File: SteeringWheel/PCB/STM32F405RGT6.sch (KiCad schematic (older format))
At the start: 21 parts, among them J14 SWD, SW1 SW_SPDT, U6 STM32F405RGT6, Y1 16MHz

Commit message: Steering Wheel Update
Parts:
- Y1: footprint Crystal:Crystal_SMD_3225-4Pin_3.2x2.5mm -> PGR-06_Additional:SODFL5326X110N
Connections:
- net BTN_CLCH: now also U6.26 (PB0); no longer U6.59 (PB7)
- net BTN_DRS: now also U6.28 (PB2); no longer U6.58 (PB6)
- net BTN_PTT: now also U6.25 (PC5); no longer U6.61 (PB8)
- net BTN_SCR: now also U6.24 (PC4); no longer U6.62 (PB9)
- net BTN_UNI1: now also U6.27 (PB1); no longer U6.57 (PB5)
- net BTN_UNI2: now also U6.37 (PC6); no longer U6.29 (PB10)
- net ROT_SCR: now also U6.15 (PA1); no longer U6.3 (PC14)
- net ROT_UNI: now also U6.14 (PA0); no longer U6.4 (PC15)
- new net I2C_RESET: U6.57 (PB5)
- new net I2C_SCL: U6.58 (PB6)
- new net I2C_SDA: U6.59 (PB7)
- no-connect marks 32 -> 31
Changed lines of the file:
@@
 $Descr A4 11693 8268
 encoding utf-8
-Sheet 2 4
+Sheet 2 3
 Title ""
 Date ""
@@
 F 0 "Y1" H 6525 4250 50  0000 L CNN
 F 1 "16MHz" H 6450 4150 50  0000 L CNN
-F 2 "Crystal:Crystal_SMD_3225-4Pin_3.2x2.5mm" H 6575 3925 50  0001 C CNN
+F 2 "PGR-06_Additional:SODFL5326X110N" H 6575 3925 50  0001 C CNN
 F 3 "~" H 6575 3925 50  0001 C CNN
 F 4 "C13738" H 6575 3925 50  0001 C CNN "LCSC Part #"
@@
 	0    -1   -1   0
 $EndComp
-NoConn ~ 3500 5475
 NoConn ~ 3500 5375
 NoConn ~ 3500 5275
 NoConn ~ 3500 5175
 NoConn ~ 3500 4875
-NoConn ~ 3500 4775
-NoConn ~ 3500 4675
-NoConn ~ 3500 4575
-NoConn ~ 3500 4475
-NoConn ~ 3500 4375
-NoConn ~ 3500 4275
 NoConn ~ 3500 4175
 NoConn ~ 3500 3975
 NoConn ~ 4900 4575
-NoConn ~ 4900 4375
-NoConn ~ 4900 3975
 NoConn ~ 4900 3475
 NoConn ~ 4900 3375
@@
 NoConn ~ 4900 2875
 NoConn ~ 4900 2775
-NoConn ~ 4900 2575
 Text GLabel 3500 3775 0    50   Input ~ 0
 HSE_OUT
@@
 Text GLabel 4900 2675 2    50   Input ~ 0
 LED_STATUS
-Text GLabel 4900 3775 2    50   Input ~ 0
-SWDIO
-Text GLabel 4900 3875 2    50   Input ~ 0
-SWCLK
 Text GLabel 4900 4475 2    50   Input ~ 0
 SWO
 Text HLabel 4900 3575 2    50   Input ~ 0
 CAN1_RX
-Text HLabel 4900 3675 2    50   Input ~ 0
-CAN1_TX
 Text HLabel 4900 5375 2    50   Input ~ 0
 CAN2_RX
 Text HLabel 4900 5475 2    50   Input ~ 0
 CAN2_TX
+Text HLabel 3500 4675 0    50   Input ~ 0
+BTN_PTT
+Text HLabel 3500 4575 0    50   Input ~ 0
+BTN_SCR
+Text HLabel 3500 4775 0    50   Input ~ 0
+BTN_UNI2
+Text HLabel 3500 4975 0    50   Input ~ 0
+LED_DATA
+NoConn ~ 3500 5075
+NoConn ~ 4900 5275
+Text HLabel 4900 4175 2    50   Input ~ 0
+BTN_CLCH
+Text HLabel 4900 4275 2    50   Input ~ 0
+BTN_UNI1
+Text HLabel 4900 4375 2    50   Input ~ 0
+BTN_DRS
 Text HLabel 4900 4775 2    50   Input ~ 0
-BTN_DRS
+I2C_SCL
 Text HLabel 4900 4875 2    50   Input ~ 0
-BTN_CLCH
-Text HLabel 4900 4975 2    50   Input ~ 0
-BTN_PTT
-Text HLabel 4900 5075 2    50   Input ~ 0
-BTN_SCR
+I2C_SDA
+Text HLabel 4900 4675 2    50   Input ~ 0
+I2C_RESET
+Text HLabel 4900 3675 2    50   Input ~ 0
+CAN1_TX
+Text GLabel 4900 3875 2    50   Input ~ 0
+SWCLK
+Text GLabel 4900 3775 2    50   Input ~ 0
+SWDIO
+NoConn ~ 4900 3975
 $Comp
 L MCU_ST_STM32F4:STM32F405RGTx U6
@@
 	1    0    0    -1
 $EndComp
-Text HLabel 4900 4675 2    50   Input ~ 0
-BTN_UNI1
-Text HLabel 4900 5175 2    50   Input ~ 0
-BTN_UNI2
-Text HLabel 3500 5575 0    50   Input ~ 0
+Text HLabel 4900 2475 2    50   Input ~ 0
+ROT_UNI
+Text HLabel 4900 2575 2    50   Input ~ 0
 ROT_SCR
-Text HLabel 3500 5675 0    50   Input ~ 0
-ROT_UNI
-Text HLabel 3500 4975 0    50   Input ~ 0
-LED_DATA
-NoConn ~ 3500 5075
-NoConn ~ 4900 5275
-NoConn ~ 4900 4175
-NoConn ~ 4900 4275
+NoConn ~ 3500 5475
+NoConn ~ 4900 4975
+NoConn ~ 4900 5075
+NoConn ~ 4900 5175
+NoConn ~ 3500 5575
+NoConn ~ 3500 5675
+NoConn ~ 3500 4275
+NoConn ~ 3500 4375
+NoConn ~ 3500 4475
+NoConn ~ 4900 3075
+Text HLabel 4200 2250 1    50   Input ~ 0
+VDD
+Text HLabel 4200 5900 3    50   Input ~ 0
+VSS
 $EndSCHEMATC

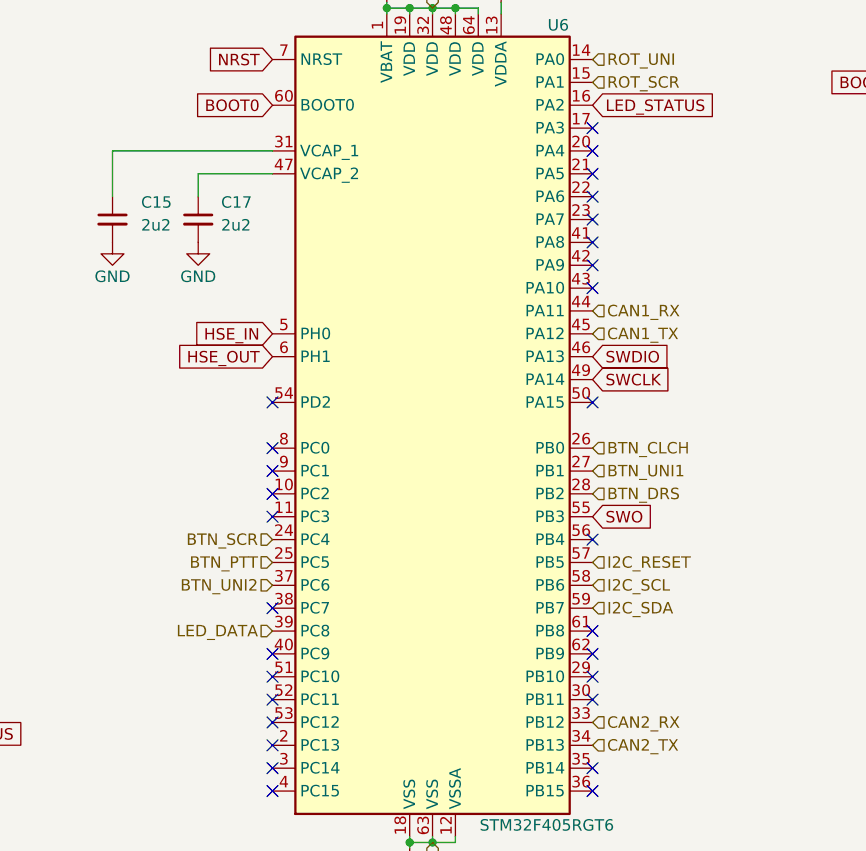
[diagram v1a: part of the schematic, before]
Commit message: New brd for steering wheel
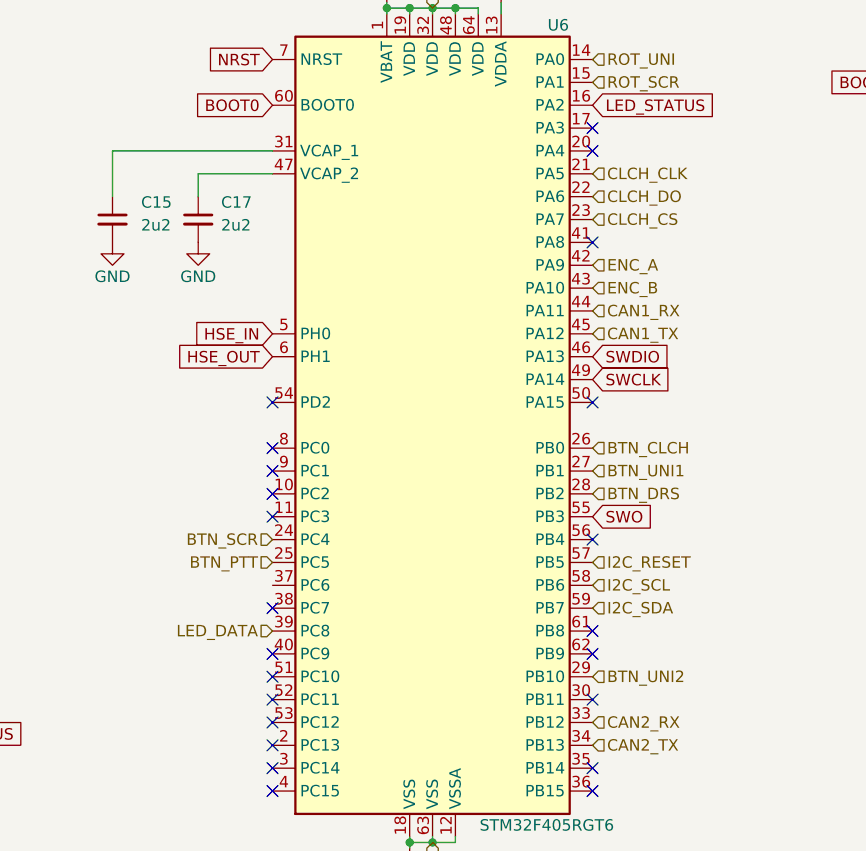
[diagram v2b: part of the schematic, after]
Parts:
- C15, C16, C17: footprint Capacitor_SMD:C_0603_1608Metric -> Capacitor_SMD:C_0805_2012Metric
- C18, C19, C20, C21, C22, C23, C24, C25, C26: footprint Capacitor_SMD:C_0402_1005Metric -> Capacitor_SMD:C_0805_2012Metric
- R15: footprint Resistor_SMD:R_0603_1608Metric -> Resistor_SMD:R_0805_2012Metric
- R16, R17: footprint Resistor_SMD:R_0402_1005Metric -> Resistor_SMD:R_0805_2012Metric
- Y1: footprint PGR-06_Additional:SODFL5326X110N -> PGR-06_Additional:OSCCC500X320X110-4N
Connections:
- net BTN_UNI2: now also U6.29 (PB10); no longer U6.37 (PC6)
- net CLCH_CLK: now reaches U6.21 (PA5)
- net CLCH_DO: now reaches U6.22 (PA6)
- net CLCH_CS: now reaches U6.23 (PA7)
- net ENC_A: now reaches U6.42 (PA9)
- net ENC_B: now reaches U6.43 (PA10)
- no-connect marks 31 -> 25
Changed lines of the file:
@@
 $Descr A4 11693 8268
 encoding utf-8
-Sheet 2 3
+Sheet 3 3
 Title ""
 Date ""
@@
 F 0 "R16" V 6300 2575 50  0000 C CNN
 F 1 "10k" V 6450 2575 50  0000 C CNN
-F 2 "Resistor_SMD:R_0402_1005Metric" H 6375 2575 50  0001 C CNN
+F 2 "Resistor_SMD:R_0805_2012Metric" H 6375 2575 50  0001 C CNN
 F 3 "~" H 6375 2575 50  0001 C CNN
 F 4 "C25744" H 6375 2575 50  0001 C CNN "LCSC Part #"
@@
 F 0 "C16" H 3175 1525 50  0000 L CNN
 F 1 "4u7" H 3175 1425 50  0000 L CNN
-F 2 "Capacitor_SMD:C_0603_1608Metric" H 3075 1475 50  0001 C CNN
+F 2 "Capacitor_SMD:C_0805_2012Metric" H 3075 1475 50  0001 C CNN
 F 3 "~" H 3075 1475 50  0001 C CNN
 F 4 "C19666" H 3075 1475 50  0001 C CNN "LCSC Part #"
@@
 F 0 "C18" H 3525 1525 50  0000 L CNN
 F 1 "100n" H 3525 1425 50  0000 L CNN
-F 2 "Capacitor_SMD:C_0402_1005Metric" H 3425 1475 50  0001 C CNN
+F 2 "Capacitor_SMD:C_0805_2012Metric" H 3425 1475 50  0001 C CNN
 F 3 "~" H 3425 1475 50  0001 C CNN
 F 4 "C1525" H 3425 1475 50  0001 C CNN "LCSC Part #"
@@
 F 0 "C19" H 3900 1525 50  0000 L CNN
 F 1 "100n" H 3900 1425 50  0000 L CNN
-F 2 "Capacitor_SMD:C_0402_1005Metric" H 3800 1475 50  0001 C CNN
+F 2 "Capacitor_SMD:C_0805_2012Metric" H 3800 1475 50  0001 C CNN
 F 3 "~" H 3800 1475 50  0001 C CNN
 F 4 "C1525" H 3800 1475 50  0001 C CNN "LCSC Part #"
@@
 F 0 "C20" H 4275 1525 50  0000 L CNN
 F 1 "100n" H 4275 1425 50  0000 L CNN
-F 2 "Capacitor_SMD:C_0402_1005Metric" H 4175 1475 50  0001 C CNN
+F 2 "Capacitor_SMD:C_0805_2012Metric" H 4175 1475 50  0001 C CNN
 F 3 "~" H 4175 1475 50  0001 C CNN
 F 4 "C1525" H 4175 1475 50  0001 C CNN "LCSC Part #"
@@
 F 0 "C21" H 4650 1525 50  0000 L CNN
 F 1 "100n" H 4650 1425 50  0000 L CNN
-F 2 "Capacitor_SMD:C_0402_1005Metric" H 4550 1475 50  0001 C CNN
+F 2 "Capacitor_SMD:C_0805_2012Metric" H 4550 1475 50  0001 C CNN
 F 3 "~" H 4550 1475 50  0001 C CNN
 F 4 "C1525" H 4550 1475 50  0001 C CNN "LCSC Part #"
@@
 F 0 "C22" H 5025 1525 50  0000 L CNN
 F 1 "100n" H 5025 1425 50  0000 L CNN
-F 2 "Capacitor_SMD:C_0402_1005Metric" H 4925 1475 50  0001 C CNN
+F 2 "Capacitor_SMD:C_0805_2012Metric" H 4925 1475 50  0001 C CNN
 F 3 "~" H 4925 1475 50  0001 C CNN
 F 4 "C1525" H 4925 1475 50  0001 C CNN "LCSC Part #"
@@
 F 0 "C23" H 6175 1525 50  0000 L CNN
 F 1 "1u" H 6175 1425 50  0000 L CNN
-F 2 "Capacitor_SMD:C_0402_1005Metric" H 6075 1475 50  0001 C CNN
+F 2 "Capacitor_SMD:C_0805_2012Metric" H 6075 1475 50  0001 C CNN
 F 3 "~" H 6075 1475 50  0001 C CNN
 F 4 "C52923" H 6075 1475 50  0001 C CNN "LCSC Part #"
@@
 F 0 "C25" H 6500 1525 50  0000 L CNN
 F 1 "10n" H 6500 1425 50  0000 L CNN
-F 2 "Capacitor_SMD:C_0402_1005Metric" H 6400 1475 50  0001 C CNN
+F 2 "Capacitor_SMD:C_0805_2012Metric" H 6400 1475 50  0001 C CNN
 F 3 "~" H 6400 1475 50  0001 C CNN
 F 4 "C15195" H 6400 1475 50  0001 C CNN "LCSC Part #"
@@
 F 0 "Y1" H 6525 4250 50  0000 L CNN
 F 1 "16MHz" H 6450 4150 50  0000 L CNN
-F 2 "PGR-06_Additional:SODFL5326X110N" H 6575 3925 50  0001 C CNN
+F 2 "PGR-06_Additional:OSCCC500X320X110-4N" H 6575 3925 50  0001 C CNN
 F 3 "~" H 6575 3925 50  0001 C CNN
 F 4 "C13738" H 6575 3925 50  0001 C CNN "LCSC Part #"
@@
 F 0 "C26" H 6925 4250 50  0000 L CNN
 F 1 "12p" H 6925 4150 50  0000 L CNN
-F 2 "Capacitor_SMD:C_0402_1005Metric" H 6825 4175 50  0001 C CNN
+F 2 "Capacitor_SMD:C_0805_2012Metric" H 6825 4175 50  0001 C CNN
 F 3 "~" H 6825 4175 50  0001 C CNN
 F 4 "C1547" H 6825 4175 50  0001 C CNN "LCSC Part #"
@@
 F 0 "C24" H 6425 4250 50  0000 L CNN
 F 1 "12p" H 6425 4150 50  0000 L CNN
-F 2 "Capacitor_SMD:C_0402_1005Metric" H 6325 4175 50  0001 C CNN
+F 2 "Capacitor_SMD:C_0805_2012Metric" H 6325 4175 50  0001 C CNN
 F 3 "~" H 6325 4175 50  0001 C CNN
 F 4 "C1547" H 6325 4175 50  0001 C CNN "LCSC Part #"
@@
 F 0 "R17" H 6900 3700 50  0000 L CNN
 F 1 "47" H 6900 3600 50  0000 L CNN
-F 2 "Resistor_SMD:R_0402_1005Metric" H 6825 3650 50  0001 C CNN
+F 2 "Resistor_SMD:R_0805_2012Metric" H 6825 3650 50  0001 C CNN
 F 3 "~" H 6825 3650 50  0001 C CNN
 F 4 "C25118" H 6825 3650 50  0001 C CNN "LCSC Part #"
@@
 F 0 "R15" H 1675 5875 50  0000 C CNN
 F 1 "1k5" H 1650 5975 50  0000 C CNN
-F 2 "Resistor_SMD:R_0603_1608Metric" H 1775 5925 50  0001 C CNN
+F 2 "Resistor_SMD:R_0805_2012Metric" H 1775 5925 50  0001 C CNN
 F 3 "~" H 1775 5925 50  0001 C CNN
 F 4 "C22843" H 1775 5925 50  0001 C CNN "LCSC Part #"
@@
 NoConn ~ 3500 3975
 NoConn ~ 4900 4575
-NoConn ~ 4900 3475
-NoConn ~ 4900 3375
 NoConn ~ 4900 3275
-NoConn ~ 4900 3175
-NoConn ~ 4900 2975
-NoConn ~ 4900 2875
 NoConn ~ 4900 2775
 Text GLabel 3500 3775 0    50   Input ~ 0
@@
 F 0 "C15" H 2925 3250 50  0000 L CNN
 F 1 "2u2" H 2925 3150 50  0000 L CNN
-F 2 "Capacitor_SMD:C_0603_1608Metric" H 2800 3175 50  0001 C CNN
+F 2 "Capacitor_SMD:C_0805_2012Metric" H 2800 3175 50  0001 C CNN
 F 3 "~" H 2800 3175 50  0001 C CNN
 F 4 "C23630" H 2800 3175 50  0001 C CNN "LCSC Part #"
@@
 F 0 "C17" H 3275 3250 50  0000 L CNN
 F 1 "2u2" H 3275 3150 50  0000 L CNN
-F 2 "Capacitor_SMD:C_0603_1608Metric" H 3175 3175 50  0001 C CNN
+F 2 "Capacitor_SMD:C_0805_2012Metric" H 3175 3175 50  0001 C CNN
 F 3 "~" H 3175 3175 50  0001 C CNN
 F 4 "C23630" H 3175 3175 50  0001 C CNN "LCSC Part #"
@@
 Text HLabel 3500 4575 0    50   Input ~ 0
 BTN_SCR
-Text HLabel 3500 4775 0    50   Input ~ 0
+Text HLabel 4900 5175 2    50   Input ~ 0
 BTN_UNI2
 Text HLabel 3500 4975 0    50   Input ~ 0
@@
 NoConn ~ 4900 4975
 NoConn ~ 4900 5075
-NoConn ~ 4900 5175
 NoConn ~ 3500 5575
 NoConn ~ 3500 5675
@@
 NoConn ~ 3500 4375
 NoConn ~ 3500 4475
-NoConn ~ 4900 3075
 Text HLabel 4200 2250 1    50   Input ~ 0
 VDD
 Text HLabel 4200 5900 3    50   Input ~ 0
 VSS
+Text HLabel 4900 3375 2    50   Input ~ 0
+ENC_A
+Text HLabel 4900 3475 2    50   Input ~ 0
+ENC_B
+NoConn ~ 4900 2875
+Text HLabel 4900 3075 2    50   Input ~ 0
+CLCH_DO
+Text HLabel 4900 2975 2    50   Input ~ 0
+CLCH_CLK
+Text HLabel 4900 3175 2    50   Input ~ 0
+CLCH_CS
 $EndSCHEMATC

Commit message: Steering Wheel Update
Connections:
- net ROT_SCR: now also U6.41 (PA8); no longer U6.15 (PA1)
- net ROT_UNI: now also U6.40 (PC9); no longer U6.14 (PA0)
- net LED_B: now reaches U6.35 (PB14)
- net LED_G: now reaches U6.36 (PB15)
- net LED_R: now reaches U6.37 (PC6)
- net LED_DATA: no longer names the net of U6.39 (PC8)
- no-connect marks 25 -> 24
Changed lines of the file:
@@
 NoConn ~ 3500 5175
 NoConn ~ 3500 4875
-NoConn ~ 3500 4175
 NoConn ~ 3500 3975
 NoConn ~ 4900 4575
-NoConn ~ 4900 3275
 NoConn ~ 4900 2775
 Text GLabel 3500 3775 0    50   Input ~ 0
@@
 	1    0    0    -1
 $EndComp
-NoConn ~ 4900 5575
-NoConn ~ 4900 5675
 $Comp
 L power:+3.3V #PWR031
@@
 Text HLabel 3500 4675 0    50   Input ~ 0
 BTN_PTT
-Text HLabel 3500 4575 0    50   Input ~ 0
-BTN_SCR
 Text HLabel 4900 5175 2    50   Input ~ 0
 BTN_UNI2
-Text HLabel 3500 4975 0    50   Input ~ 0
-LED_DATA
-NoConn ~ 3500 5075
 NoConn ~ 4900 5275
 Text HLabel 4900 4175 2    50   Input ~ 0
@@
 SWDIO
 NoConn ~ 4900 3975
-$Comp
-L MCU_ST_STM32F4:STM32F405RGTx U6
-U 1 1 61927F05
-P 4200 4075
-F 0 "U6" H 4750 5825 50  0000 C CNN
-F 1 "STM32F405RGT6" H 4700 2325 50  0000 C CNN
-F 2 "Package_QFP:LQFP-64_10x10mm_P0.5mm" H 3600 2375 50  0001 R CNN
-F 3 "http://www.st.com/st-web-ui/static/active/en/resource/technical/document/datasheet/DM00037051.pdf" H 4200 4075 50  0001 C CNN
-F 4 "C15742" H 4200 4075 50  0001 C CNN "LCSC Part #"
-	1    4200 4075
-	1    0    0    -1
-$EndComp
-Text HLabel 4900 2475 2    50   Input ~ 0
+Text HLabel 3500 5075 0    50   Input ~ 0
 ROT_UNI
-Text HLabel 4900 2575 2    50   Input ~ 0
+Text HLabel 4900 3275 2    50   Input ~ 0
 ROT_SCR
 NoConn ~ 3500 5475
@@
 NoConn ~ 3500 5575
 NoConn ~ 3500 5675
-NoConn ~ 3500 4275
-NoConn ~ 3500 4375
 NoConn ~ 3500 4475
 Text HLabel 4200 2250 1    50   Input ~ 0
@@
 Text HLabel 4900 3175 2    50   Input ~ 0
 CLCH_CS
+Text HLabel 3500 4575 0    50   Input ~ 0
+BTN_SCR
+NoConn ~ 4900 2575
+NoConn ~ 4900 2475
+$Comp
+L MCU_ST_STM32F4:STM32F405RGTx U6
+U 1 1 61927F05
+P 4200 4075
+F 0 "U6" H 4750 5825 50  0000 C CNN
+F 1 "STM32F405RGT6" H 4700 2325 50  0000 C CNN
+F 2 "Package_QFP:LQFP-64_10x10mm_P0.5mm" H 3600 2375 50  0001 R CNN
+F 3 "http://www.st.com/st-web-ui/static/active/en/resource/technical/document/datasheet/DM00037051.pdf" H 4200 4075 50  0001 C CNN
+F 4 "C15742" H 4200 4075 50  0001 C CNN "LCSC Part #"
+	1    4200 4075
+	1    0    0    -1
+$EndComp
+Text HLabel 3500 4775 0    50   Input ~ 0
+LED_R
+Text HLabel 4900 5675 2    50   Input ~ 0
+LED_G
+Text HLabel 4900 5575 2    50   Input ~ 0
+LED_B
+NoConn ~ 3500 4975
+NoConn ~ 3500 4175
+NoConn ~ 3500 4275
+NoConn ~ 3500 4375
 $EndSCHEMATC
